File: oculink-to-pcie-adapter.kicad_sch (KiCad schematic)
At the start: 0 parts

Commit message: [#79026] Add OCuLink and PCIex16 connectors, connect them together
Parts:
- added MP1, MP2, MP3, MP4: MP_Pad6mm_Drill3.2mm, antmicro-footprints:MP_Pad6mm_Drill3.2mm, symbol antmicroMechanicalParts:MP_Pad6mm_Drill3.2mm
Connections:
- new net GND: MP1.1, MP2.1, MP3.1, MP4.1
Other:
- added sheet OCuLink (oculink.kicad_sch)
- added sheet PCIe-connector (pcie-connector.kicad_sch)
- added sheet Power (power.kicad_sch)

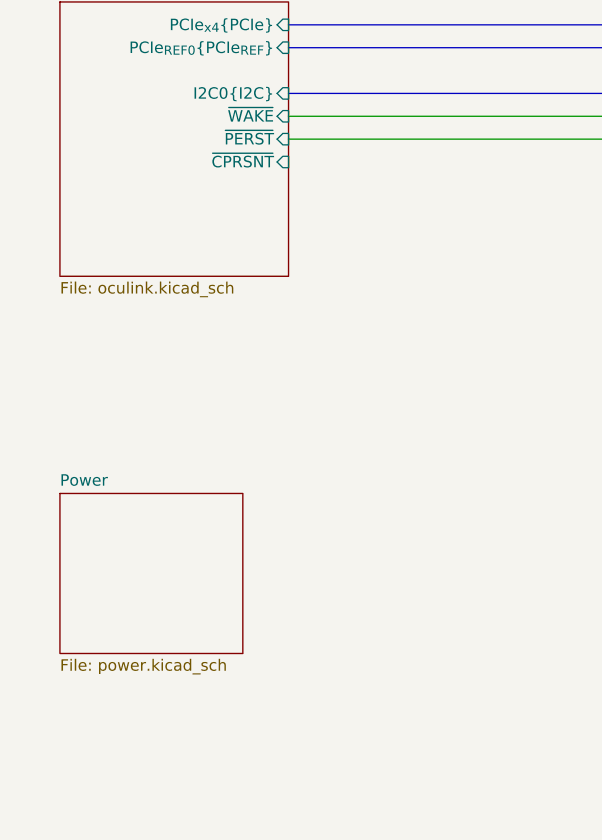
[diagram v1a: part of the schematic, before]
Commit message: [#79026] Add power supply section, reannotate schematic
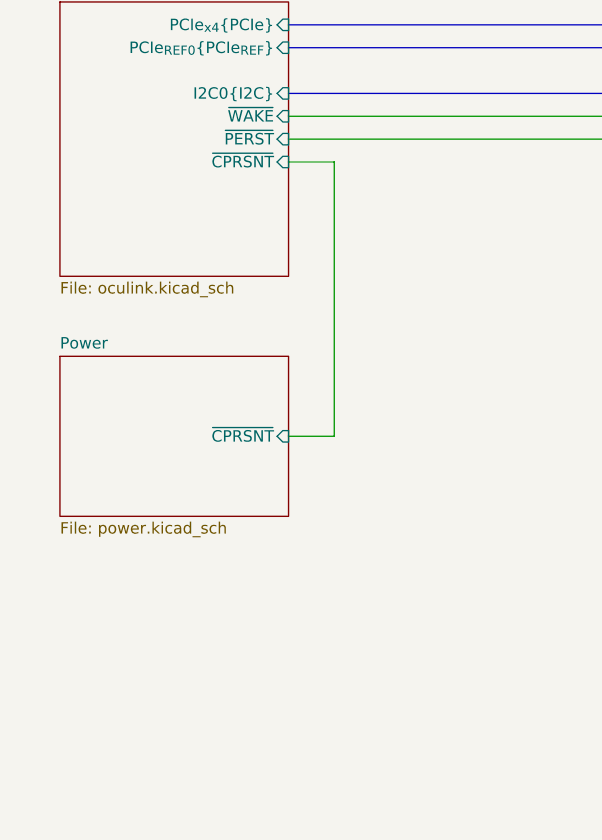
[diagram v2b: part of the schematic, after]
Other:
- sheet Power ports: added ~{CPRSNT}; removed none
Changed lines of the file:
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@@
+	(wire
+		(pts
+			(xy 142.24 142.24) (xy 137.16 142.24)
+		)
+		(stroke
+			(width 0)
+			(type default)
+		)
+	)
 	(wire
 		(pts
@@
 		)
 	)
+	(wire
+		(pts
+			(xy 137.16 172.72) (xy 142.24 172.72)
+		)
+		(stroke
+			(width 0)
+			(type default)
+		)
+	)
 	(bus
 		(pts
 			(xy 137.16 127) (xy 273.05 127)
+		)
+		(stroke
+			(width 0)
+			(type default)
+		)
+	)
+	(wire
+		(pts
+			(xy 142.24 172.72) (xy 142.24 142.24)
 		)
 		(stroke
@@
 	)
 	(sheet
-		(at 111.76 179.07)
-		(size 20.32 17.78)
+		(at 111.76 163.83)
+		(size 25.4 17.78)
 		(exclude_from_sim no)
 		(in_bom yes)
@@
 		)
 		(property "Sheetname" "Power"
-			(at 111.76 178.3584 0)
+			(at 111.76 163.1184 0)
 			(effects
 				(font
@@
 		)
 		(property "Sheetfile" "power.kicad_sch"
-			(at 111.76 197.4346 0)
+			(at 111.76 182.1946 0)
 			(effects
 				(font
@@
 			)
 		)
+		(pin "~{CPRSNT}" input
+			(at 137.16 172.72 0)
+			(effects
+				(font
+					(size 1.27 1.27)
+				)
+				(justify right)
+			)
+		)

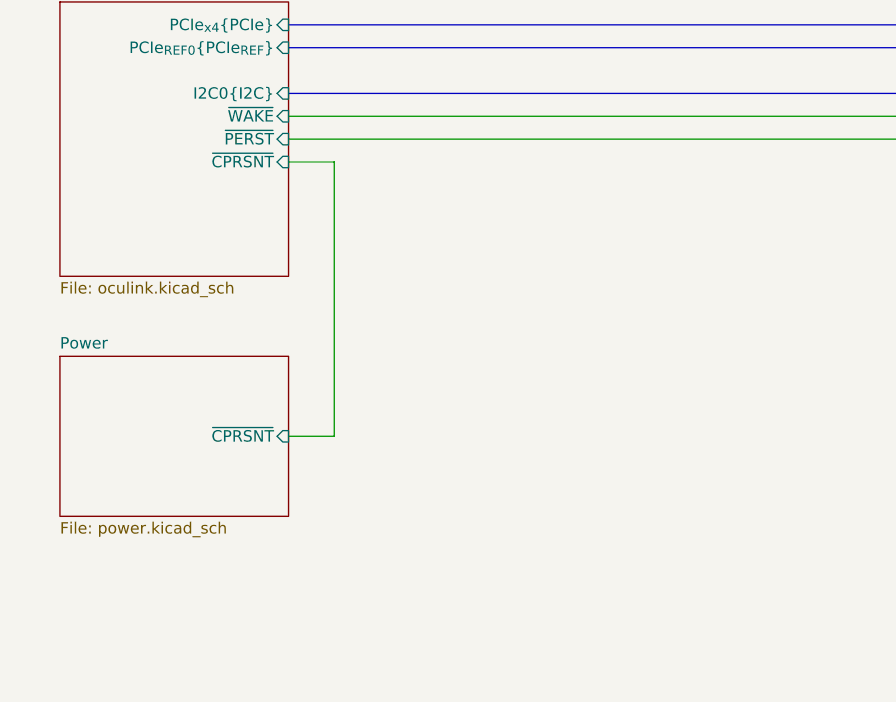
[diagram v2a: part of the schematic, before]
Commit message: [#79262] Add USB PD input, 12V DC-DC converter, power ORing
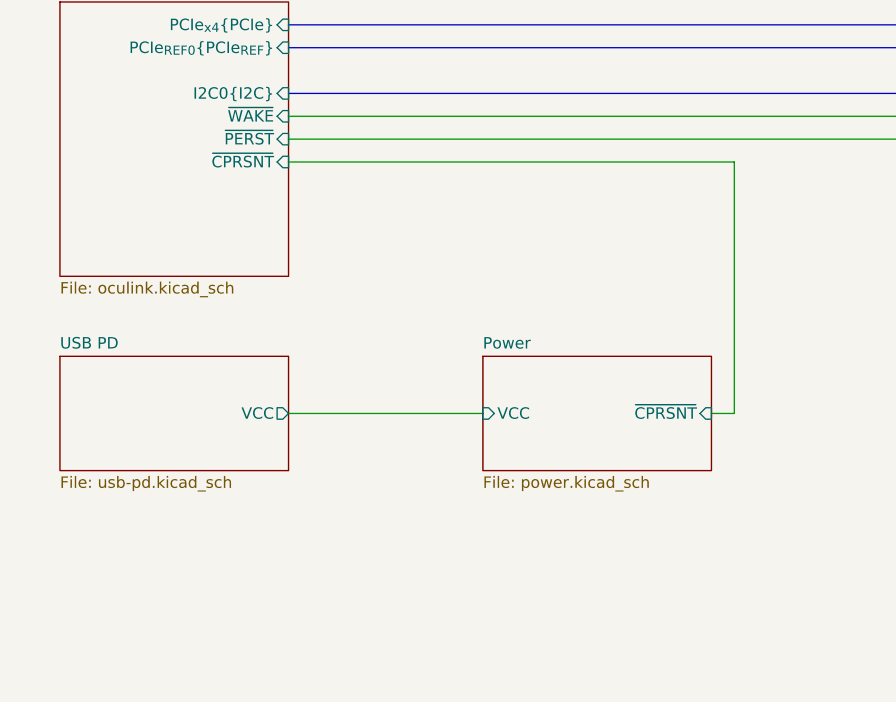
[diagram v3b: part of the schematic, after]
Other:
- added sheet USB PD (usb-pd.kicad_sch)
- sheet Power ports: added VCC; removed none
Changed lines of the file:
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@@
 	(wire
 		(pts
-			(xy 142.24 142.24) (xy 137.16 142.24)
+			(xy 186.69 142.24) (xy 137.16 142.24)
 		)
 		(stroke
@@
 	(wire
 		(pts
+			(xy 137.16 170.18) (xy 158.75 170.18)
+		)
+		(stroke
+			(width 0)
+			(type default)
+		)
+	)
+	(wire
+		(pts
 			(xy 367.03 214.63) (xy 364.49 214.63)
 		)
@@
 	(wire
 		(pts
-			(xy 137.16 172.72) (xy 142.24 172.72)
+			(xy 184.15 170.18) (xy 186.69 170.18)
 		)
 		(stroke
@@
 	(wire
 		(pts
-			(xy 142.24 172.72) (xy 142.24 142.24)
+			(xy 186.69 170.18) (xy 186.69 142.24)
 		)
 		(stroke
@@
 	)
 	(sheet
-		(at 111.76 163.83)
-		(size 25.4 17.78)
+		(at 158.75 163.83)
+		(size 25.4 12.7)
 		(exclude_from_sim no)
 		(in_bom yes)
@@
 		)
 		(property "Sheetname" "Power"
-			(at 111.76 163.1184 0)
+			(at 158.75 163.1184 0)
 			(effects
 				(font
@@
 		)
 		(property "Sheetfile" "power.kicad_sch"
-			(at 111.76 182.1946 0)
+			(at 158.75 177.1146 0)
 			(effects
 				(font
@@
 		)
 		(pin "~{CPRSNT}" input
-			(at 137.16 172.72 0)
+			(at 184.15 170.18 0)
 			(effects
 				(font
@@
 				)
 				(justify right)
+			)
+		)
+		(pin "VCC" input
+			(at 158.75 170.18 180)
+			(effects
+				(font
+					(size 1.27 1.27)
+				)
+				(justify left)
 			)
 		)
@@
 				)
 			)
+		)
+	)
+	(sheet
+		(at 111.76 163.83)
+		(size 25.4 12.7)
+		(exclude_from_sim no)
+		(in_bom yes)
+		(on_board yes)
+		(dnp no)
+		(fields_autoplaced yes)
+		(stroke
+			(width 0.1524)
+			(type solid)
+		)
+		(fill
+			(color 0 0 0 0.0000)
+		)
+		(property "Sheetname" "USB PD"
+			(at 111.76 163.1184 0)
+			(effects
+				(font
+					(size 1.27 1.27)
+				)
+				(justify left bottom)
+			)
+		)
+		(property "Sheetfile" "usb-pd.kicad_sch"
+			(at 111.76 177.1146 0)
+			(effects
+				(font
+					(size 1.27 1.27)
+				)
+				(justify left top)
+			)
+		)
+		(pin "VCC" output
+			(at 137.16 170.18 0)
+			(effects
+				(font
+					(size 1.27 1.27)
+				)
+				(justify right)
+			)
+		)
+		(instances
+			(project "oculink-to-pcie-adapter"
+				(path "/44c3be85-0a18-4d93-a9a5-650ee09b6032"
+					(page "5")
+				)
+			)

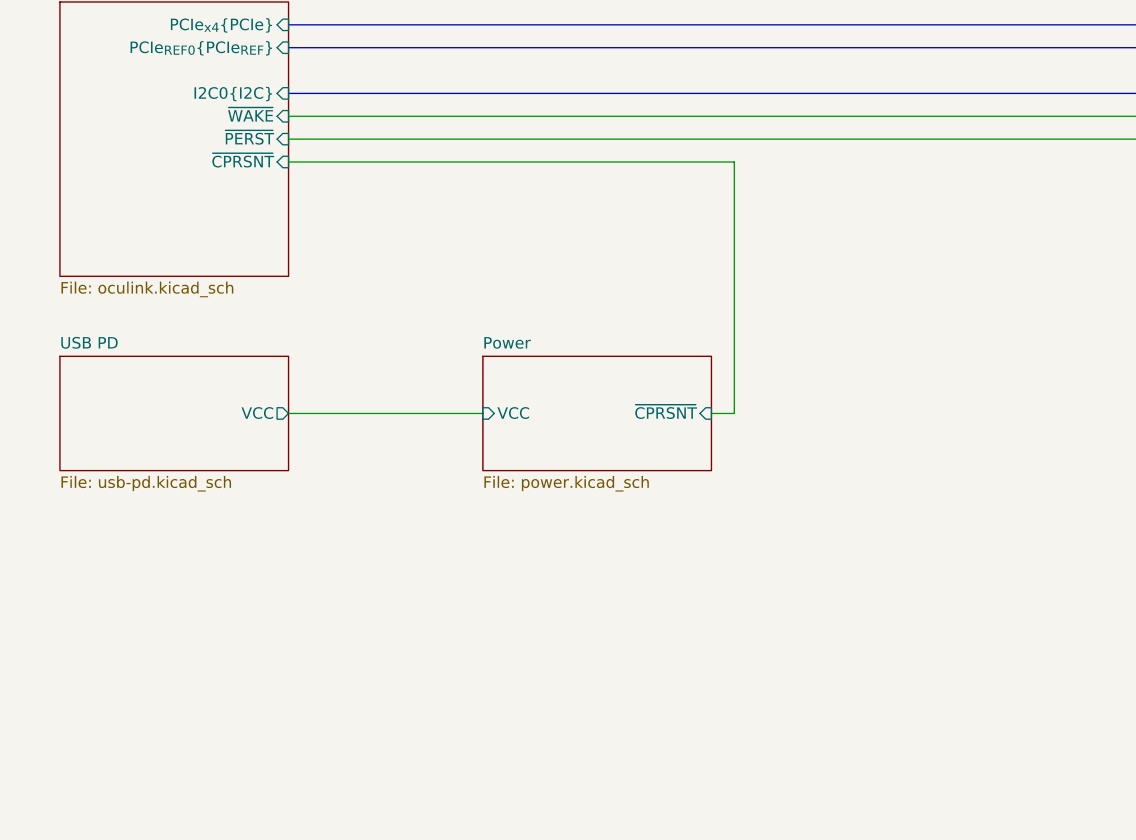
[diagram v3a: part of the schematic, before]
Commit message: [#79262] Move ideal diodes and Molex connector to separate schematic sheet
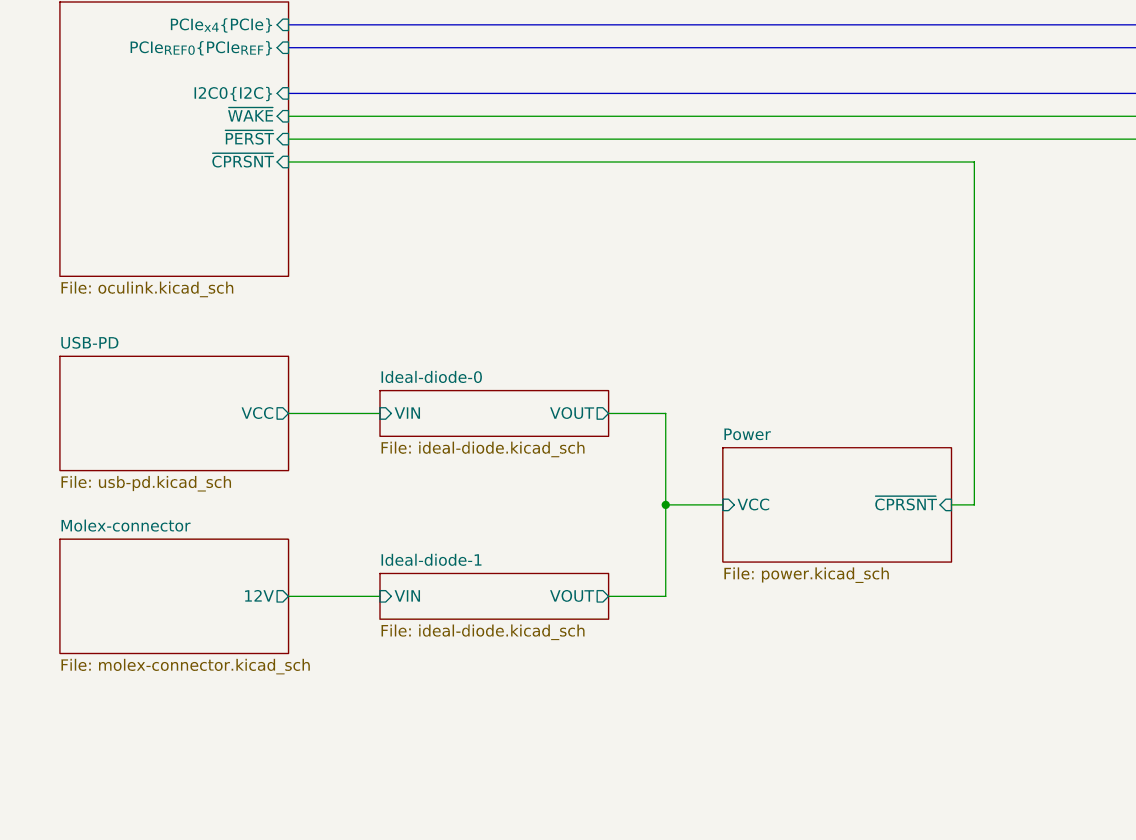
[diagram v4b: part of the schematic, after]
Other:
- sheet USB PD renamed USB-PD
- added sheet Ideal-diode-0 (ideal-diode.kicad_sch)
- added sheet Ideal-diode-1 (ideal-diode.kicad_sch)
- added sheet Molex-connector (molex-connector.kicad_sch)

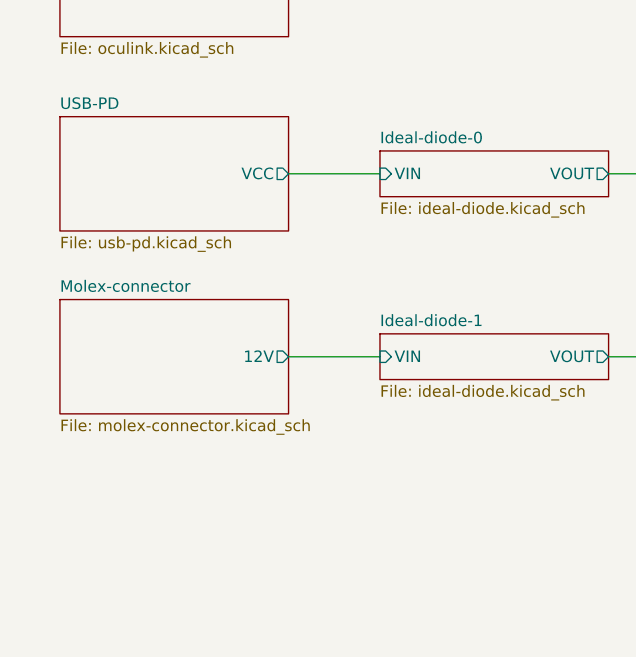
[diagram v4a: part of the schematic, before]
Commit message: [#79262] Cleanup 12V DC-DC converter, move Molex connector to root sheet
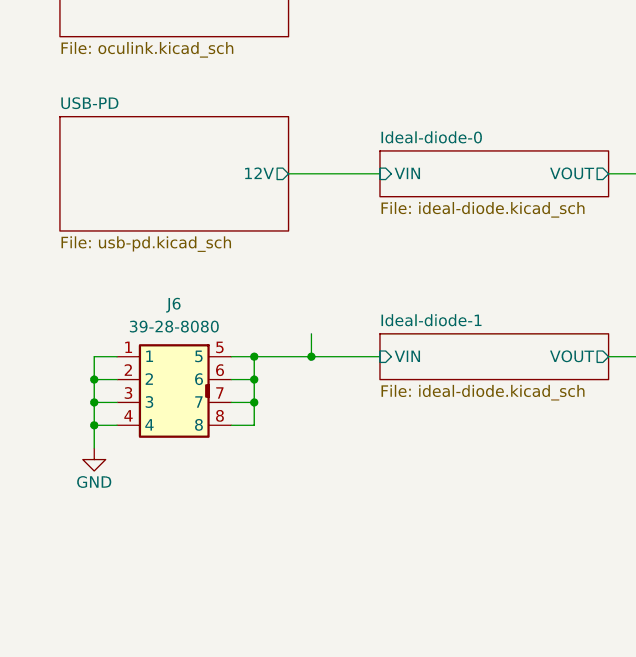
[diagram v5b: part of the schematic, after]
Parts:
- added J6: Molex_Mini-Fit-Jr_2x4_39-28-8080, antmicro-footprints:MOLEX_39288080, symbol antmicroWire2BoardConnectors:Molex_Mini-Fit-Jr_2x4_39-28-8080
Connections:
- net GND: now also J6.1, J6.2, J6.3, J6.4
- net Ideal-diode-1/VIN: now also J6.5, J6.6, J6.7, J6.8
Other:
- removed sheet Molex-connector
- sheet USB-PD ports: added 12V; removed VCC

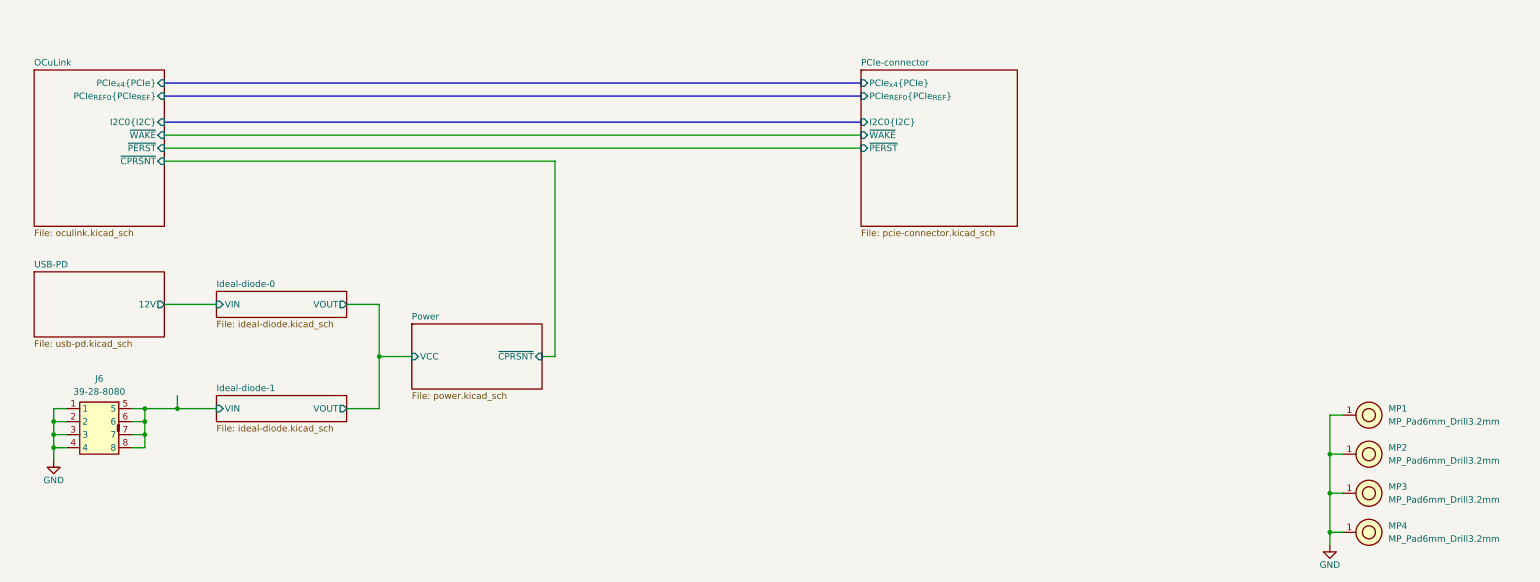
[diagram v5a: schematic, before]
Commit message: [#79262] Finish power section schematic
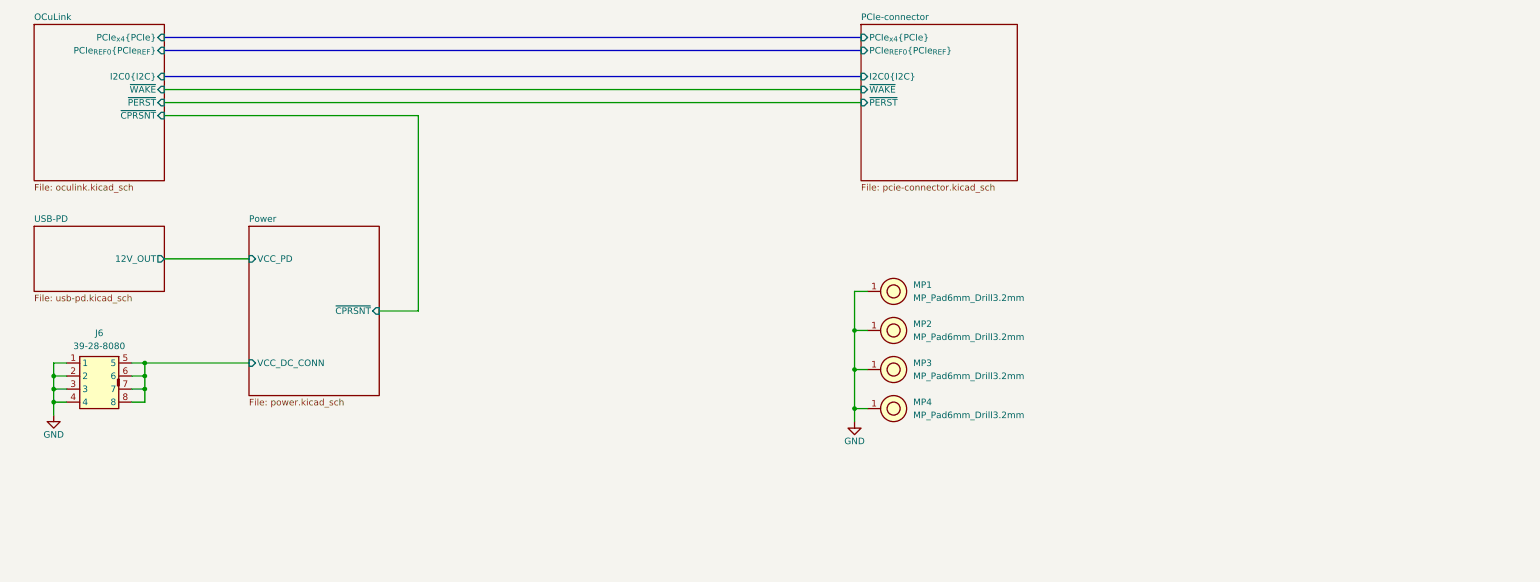
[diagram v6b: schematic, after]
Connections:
- net Ideal-diode-1/VIN renamed Power/VCC_DC_CONN
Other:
- removed sheet Ideal-diode-0
- removed sheet Ideal-diode-1
- sheet Power ports: added VCC_DC_CONN, VCC_PD; removed VCC
- sheet USB-PD ports: added 12V_OUT; removed 12V
- moved on the sheet: J6, MP1, MP2, MP3, MP4
